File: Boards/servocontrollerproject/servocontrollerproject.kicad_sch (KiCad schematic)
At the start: 4 parts, among them J1 B3B-XH-A_LF__SN_, J2 B3B-XH-A_LF__SN_, J3 USB_A, U1 ProMicro

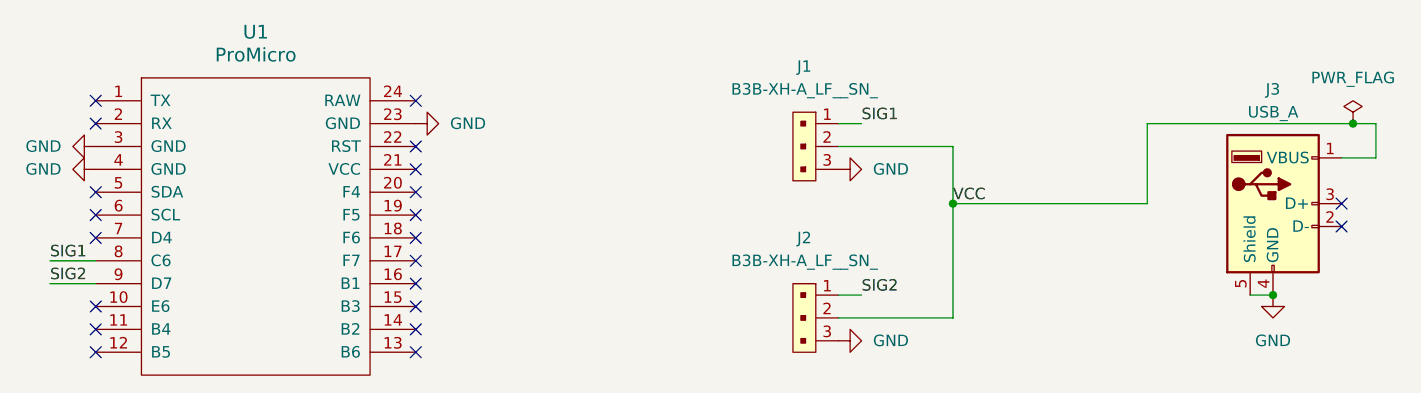
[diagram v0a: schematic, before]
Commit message: finished servo layout
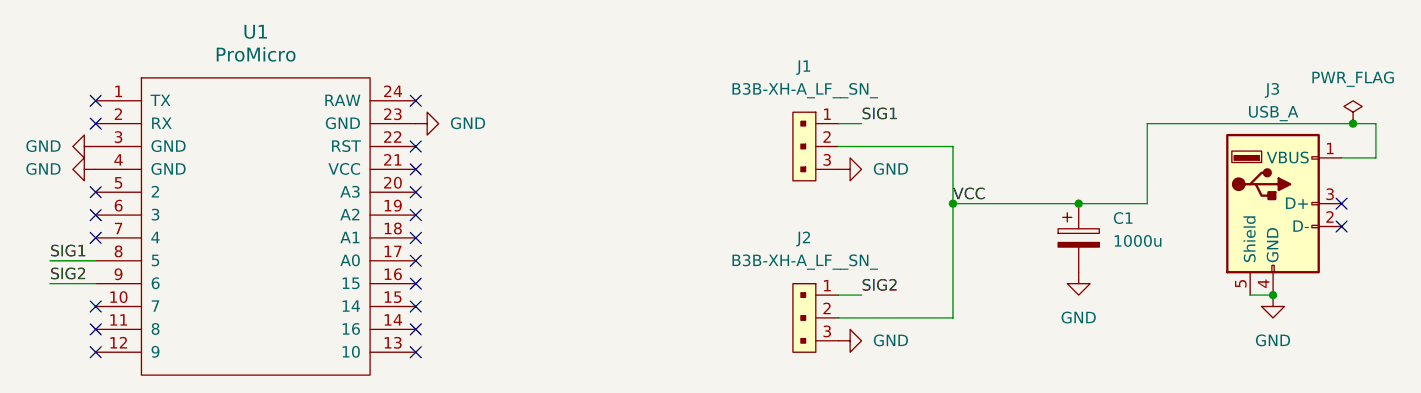
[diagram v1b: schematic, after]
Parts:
- removed U1: ProMicro, PiEParts:ProMicro, symbol promicro:ProMicro
- added C1: 1000u, Capacitor_THT:CP_Radial_D10.0mm_P5.00mm, symbol Device:C_Polarized
- added U1: ProMicro, PiE_Footprints:ProMicro-EnforcedTop, symbol PiE_Symbols:ProMicro
- J1, J2: footprint digikey-footprints:PinHeader_1x3_P2.5mm_Drill1.1mm -> Connector_PinHeader_2.54mm:PinHeader_1x03_P2.54mm_Vertical
- J3: footprint Connector_USB:USB_A_Molex_67643_Horizontal -> PiE_Footprints:USB-A_female
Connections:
- net GND: now also C1.2, U1.23 (GND), U1.3 (GND), U1.4 (GND)
- net SIG1: now also U1.8 (5)
- net SIG2: now also U1.9 (6)
- net VCC: now also C1.1

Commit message: Ordered Servo Controller
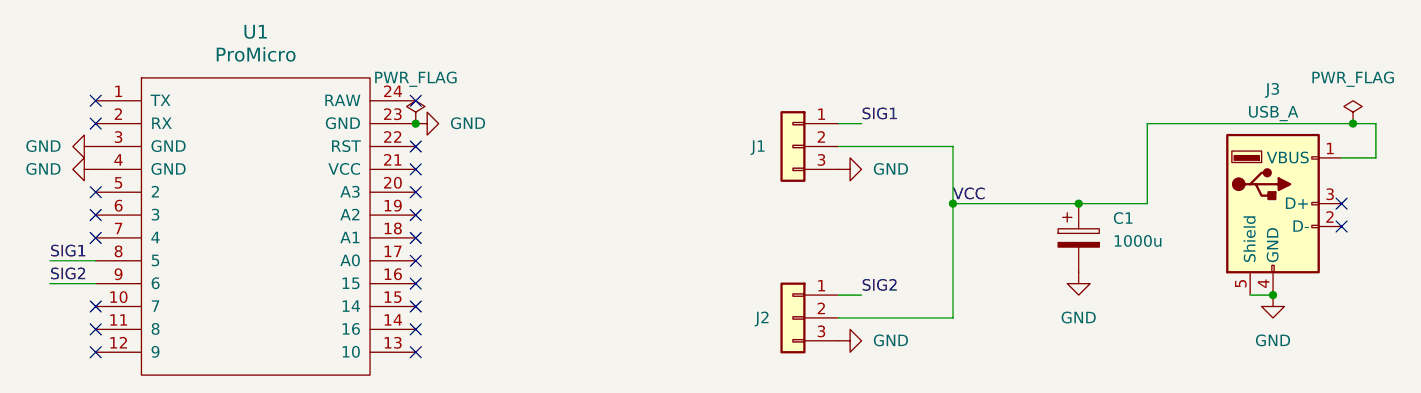
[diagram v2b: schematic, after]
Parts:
- J1, J2: value B3B-XH-A_LF__SN_ -> ~; symbol dk_Rectangular-Connectors-Headers-Male-Pins:B3B-XH-A_LF__SN_ -> Connector_Generic:Conn_01x03
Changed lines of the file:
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@@
   (junction (at 154.94 69.85) (diameter 0) (color 0 0 0 0)
+  )
+  (junction (at 95.25 60.96) (diameter 0) (color 0 0 0 0)
   )
   (junction (at 199.39 60.96) (diameter 0) (color 0 0 0 0)
@@
   (label "SIG1" (at 144.78 60.96 0) (fields_autoplaced)
     (effects (font (size 1.27 1.27)) (justify left bottom))
+  )
+  (symbol (lib_id "power:PWR_FLAG") (at 95.25 60.96 0) (unit 1)
+    (in_bom yes) (on_board yes) (dnp no) (fields_autoplaced)
+    (property "Reference" "#FLG02" (at 95.25 59.055 0)
+      (effects (font (size 1.27 1.27)) hide)
+    )
+    (property "Value" "PWR_FLAG" (at 95.25 55.88 0)
+      (effects (font (size 1.27 1.27)))
+    )
+    (property "Footprint" "" (at 95.25 60.96 0)
+      (effects (font (size 1.27 1.27)) hide)
+    )
+    (property "Datasheet" "~" (at 95.25 60.96 0)
+      (effects (font (size 1.27 1.27)) hide)
+    )
+    (pin "1")
+    (instances
+      (project "servocontrollerproject"
+        (path "/318b2e4f-4e40-4d52-b73d-37d85ea9395e"
+          (reference "#FLG02") (unit 1)
+        )
+      )
+    )
   )
   (symbol (lib_id "power:GND") (at 190.5 80.01 0) (unit 1)
@@
     )
   )
-  (symbol (lib_id "dk_Rectangular-Connectors-Headers-Male-Pins:B3B-XH-A_LF__SN_") (at 139.7 60.96 270) (unit 1)
-    (in_bom yes) (on_board yes) (dnp no) (fields_autoplaced)
-    (property "Reference" "J1" (at 138.43 54.61 90)
-      (effects (font (size 1.27 1.27)))
-    )
-    (property "Value" "B3B-XH-A_LF__SN_" (at 138.43 57.15 90)
-      (effects (font (size 1.27 1.27)))
-    )
-    (property "Footprint" "Connector_PinHeader_2.54mm:PinHeader_1x03_P2.54mm_Vertical" (at 144.78 66.04 0)
-      (effects (font (size 1.27 1.27)) (justify left) hide)
-    )
-    (property "Datasheet" "http://www.jst-mfg.com/product/pdf/eng/eXH.pdf" (at 147.32 66.04 0)
-      (effects (font (size 1.27 1.27)) (justify left) hide)
-    )
-    (property "Digi-Key_PN" "455-2248-ND" (at 149.86 66.04 0)
-      (effects (font (size 1.524 1.524)) (justify left) hide)
-    )
-    (property "MPN" "B3B-XH-A(LF)(SN)" (at 152.4 66.04 0)
-      (effects (font (size 1.524 1.524)) (justify left) hide)
-    )
-    (property "Category" "Connectors, Interconnects" (at 154.94 66.04 0)
-      (effects (font (size 1.524 1.524)) (justify left) hide)
-    )
-    (property "Family" "Rectangular Connectors - Headers, Male Pins" (at 157.48 66.04 0)
-      (effects (font (size 1.524 1.524)) (justify left) hide)
-    )
-    (property "DK_Datasheet_Link" "http://www.jst-mfg.com/product/pdf/eng/eXH.pdf" (at 160.02 66.04 0)
-      (effects (font (size 1.524 1.524)) (justify left) hide)
-    )
-    (property "DK_Detail_Page" "/product-detail/en/jst-sales-america-inc/B3B-XH-A(LF)(SN)/455-2248-ND/1651046" (at 162.56 66.04 0)
-      (effects (font (size 1.524 1.524)) (justify left) hide)
-    )
-    (property "Description" "CONN HEADER VERT 3POS 2.5MM" (at 165.1 66.04 0)
-      (effects (font (size 1.524 1.524)) (justify left) hide)
-    )
-    (property "Manufacturer" "JST Sales America Inc." (at 167.64 66.04 0)
-      (effects (font (size 1.524 1.524)) (justify left) hide)
-    )
-    (property "Status" "Active" (at 170.18 66.04 0)
+  (symbol (lib_id "Connector_Generic:Conn_01x03") (at 137.16 63.5 0) (mirror y) (unit 1)
+    (in_bom yes) (on_board yes) (dnp no)
+    (property "Reference" "J1" (at 133.35 63.5 0)
+      (effects (font (size 1.27 1.27)))
+    )
+    (property "Value" "~" (at 140.97 64.77 90)
+      (effects (font (size 1.27 1.27)))
+    )
+    (property "Footprint" "Connector_PinHeader_2.54mm:PinHeader_1x03_P2.54mm_Vertical" (at 137.16 63.5 0)
+      (effects (font (size 1.27 1.27)) hide)
+    )
+    (property "Datasheet" "~" (at 137.16 63.5 0)
+      (effects (font (size 1.27 1.27)) hide)
+    )
+    (property "Digi-Key_PN" "455-2248-ND" (at 132.08 53.34 0)
+      (effects (font (size 1.524 1.524)) (justify left) hide)
+    )
+    (property "MPN" "B3B-XH-A(LF)(SN)" (at 132.08 50.8 0)
+      (effects (font (size 1.524 1.524)) (justify left) hide)
+    )
+    (property "Category" "Connectors, Interconnects" (at 132.08 48.26 0)
+      (effects (font (size 1.524 1.524)) (justify left) hide)
+    )
+    (property "Family" "Rectangular Connectors - Headers, Male Pins" (at 132.08 45.72 0)
+      (effects (font (size 1.524 1.524)) (justify left) hide)
+    )
+    (property "DK_Datasheet_Link" "http://www.jst-mfg.com/product/pdf/eng/eXH.pdf" (at 132.08 43.18 0)
+      (effects (font (size 1.524 1.524)) (justify left) hide)
+    )
+    (property "DK_Detail_Page" "/product-detail/en/jst-sales-america-inc/B3B-XH-A(LF)(SN)/455-2248-ND/1651046" (at 132.08 40.64 0)
+      (effects (font (size 1.524 1.524)) (justify left) hide)
+    )
+    (property "Description" "CONN HEADER VERT 3POS 2.5MM" (at 132.08 38.1 0)
+      (effects (font (size 1.524 1.524)) (justify left) hide)
+    )
+    (property "Manufacturer" "JST Sales America Inc." (at 132.08 35.56 0)
+      (effects (font (size 1.524 1.524)) (justify left) hide)
+    )
+    (property "Status" "Active" (at 132.08 33.02 0)
       (effects (font (size 1.524 1.524)) (justify left) hide)
     )
@@
     )
   )
-  (symbol (lib_id "dk_Rectangular-Connectors-Headers-Male-Pins:B3B-XH-A_LF__SN_") (at 139.7 80.01 270) (unit 1)
-    (in_bom yes) (on_board yes) (dnp no) (fields_autoplaced)
-    (property "Reference" "J2" (at 138.43 73.66 90)
-      (effects (font (size 1.27 1.27)))
-    )
-    (property "Value" "B3B-XH-A_LF__SN_" (at 138.43 76.2 90)
-      (effects (font (size 1.27 1.27)))
-    )
-    (property "Footprint" "Connector_PinHeader_2.54mm:PinHeader_1x03_P2.54mm_Vertical" (at 144.78 85.09 0)
-      (effects (font (size 1.27 1.27)) (justify left) hide)
-    )
-    (property "Datasheet" "http://www.jst-mfg.com/product/pdf/eng/eXH.pdf" (at 147.32 85.09 0)
-      (effects (font (size 1.27 1.27)) (justify left) hide)
-    )
-    (property "Digi-Key_PN" "455-2248-ND" (at 149.86 85.09 0)
-      (effects (font (size 1.524 1.524)) (justify left) hide)
-    )
-    (property "MPN" "B3B-XH-A(LF)(SN)" (at 152.4 85.09 0)
-      (effects (font (size 1.524 1.524)) (justify left) hide)
-    )
-    (property "Category" "Connectors, Interconnects" (at 154.94 85.09 0)
-      (effects (font (size 1.524 1.524)) (justify left) hide)
-    )
-    (property "Family" "Rectangular Connectors - Headers, Male Pins" (at 157.48 85.09 0)
-      (effects (font (size 1.524 1.524)) (justify left) hide)
-    )
-    (property "DK_Datasheet_Link" "http://www.jst-mfg.com/product/pdf/eng/eXH.pdf" (at 160.02 85.09 0)
-      (effects (font (size 1.524 1.524)) (justify left) hide)
-    )
-    (property "DK_Detail_Page" "/product-detail/en/jst-sales-america-inc/B3B-XH-A(LF)(SN)/455-2248-ND/1651046" (at 162.56 85.09 0)
-      (effects (font (size 1.524 1.524)) (justify left) hide)
-    )
-    (property "Description" "CONN HEADER VERT 3POS 2.5MM" (at 165.1 85.09 0)
-      (effects (font (size 1.524 1.524)) (justify left) hide)
-    )
-    (property "Manufacturer" "JST Sales America Inc." (at 167.64 85.09 0)
-      (effects (font (size 1.524 1.524)) (justify left) hide)
-    )
-    (property "Status" "Active" (at 170.18 85.09 0)
-      (effects (font (size 1.524 1.524)) (justify left) hide)
-    )
+  (symbol (lib_id "Connector_Generic:Conn_01x03") (at 137.16 82.55 0) (mirror y) (unit 1)
+    (in_bom yes) (on_board yes) (dnp no) (fields_autoplaced)
+    (property "Reference" "J2" (at 134.62 82.55 0)
+      (effects (font (size 1.27 1.27)) (justify left))
+    )
+    (property "Value" "~" (at 134.62 83.82 0)
+      (effects (font (size 1.27 1.27)) (justify left))
+    )
+    (property "Footprint" "Connector_PinHeader_2.54mm:PinHeader_1x03_P2.54mm_Vertical" (at 137.16 82.55 0)
+      (effects (font (size 1.27 1.27)) hide)
+    )
+    (property "Datasheet" "~" (at 137.16 82.55 0)
+      (effects (font (size 1.27 1.27)) hide)
+    )
+    (property "Digi-Key_PN" "455-2248-ND" (at 132.08 72.39 0)
+      (effects (font (size 1.524 1.524)) (justify left) hide)
+    )
+    (property "MPN" "B3B-XH-A(LF)(SN)" (at 132.08 69.85 0)
+      (effects (font (size 1.524 1.524)) (justify left) hide)
+    )
+    (property "Category" "Connectors, Interconnects" (at 132.08 67.31 0)
+      (effects (font (size 1.524 1.524)) (justify left) hide)
+    )
+    (property "Family" "Rectangular Connectors - Headers, Male Pins" (at 132.08 64.77 0)
+      (effects (font (size 1.524 1.524)) (justify left) hide)
+    )
+    (property "DK_Datasheet_Link" "http://www.jst-mfg.com/product/pdf/eng/eXH.pdf" (at 132.08 62.23 0)
+      (effects (font (size 1.524 1.524)) (justify left) hide)
+    )
+    (property "DK_Detail_Page" "/product-detail/en/jst-sales-america-inc/B3B-XH-A(LF)(SN)/455-2248-ND/1651046" (at 132.08 59.69 0)
+      (effects (font (size 1.524 1.524)) (justify left) hide)
+    )
+    (property "Description" "CONN HEADER VERT 3POS 2.5MM" (at 132.08 57.15 0)
+      (effects (font (size 1.524 1.524)) (justify left) hide)
+    )
+    (property "Manufacturer" "JST Sales America Inc." (at 132.08 54.61 0)
+      (effects (font (size 1.524 1.524)) (justify left) hide)
+    )
+    (property "Status" "Active" (at 132.08 52.07 0)
+      (effects (font (size 1.524 1.524)) (justify left) hide)
+    )
